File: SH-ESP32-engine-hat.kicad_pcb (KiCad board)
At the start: 4 copper layers, 34 x 52.8 mm, 106 parts, among them J301 Conn_02x04_Odd_Even, J302 Conn_02x04_Odd_Even, J401 I2C_top, J402 I2C_bottom, J403 GPIO subset, J501 Conn_02x04_Odd_Even, J502 Conn_02x04, Q501 S9015, Q502 S9015, Q503 S9015, Q504 S9015, U501 LMV324, U502 ADS1115IDGS

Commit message: Fix solder jumper silkscreen
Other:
- board text added: "0x48"
- board text added: "0x49"
- board text added: "0x4a"
- board text added: "0x4b"
- board text removed: "48"
- board text removed: "49"
- board text removed: "50"
- board text removed: "51"
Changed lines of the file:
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@@
     (effects (font (size 1 1) (thickness 0.16)) (justify mirror))
   )
-  (gr_text "I2C" (at 135.2 104.3) (layer "B.SilkS")
+  (gr_text "I2C" (at 135.4 104.3 270) (layer "B.SilkS")
     (effects (font (size 1 1) (thickness 0.2)) (justify mirror))
   )
@@
     (effects (font (size 0.8 0.8) (thickness 0.16)) (justify mirror))
   )
-  (gr_text "49" (at 131 97.8) (layer "B.SilkS")
+  (gr_text "0x49" (at 131 97.8) (layer "B.SilkS")
     (effects (font (size 0.8 0.8) (thickness 0.16)) (justify right mirror))
   )
-  (gr_text "51" (at 131 100.4) (layer "B.SilkS")
+  (gr_text "0x4b" (at 131 100.4) (layer "B.SilkS")
     (effects (font (size 0.8 0.8) (thickness 0.16)) (justify right mirror))
   )
-  (gr_text "48" (at 131.1 105.6) (layer "B.SilkS")
+  (gr_text "0x48" (at 131.1 105.6) (layer "B.SilkS")
     (effects (font (size 0.8 0.8) (thickness 0.16)) (justify right mirror))
   )
@@
     (effects (font (size 1 1) (thickness 0.2)) (justify mirror))
   )
-  (gr_text "50" (at 131 103) (layer "B.SilkS")
+  (gr_text "0x4a" (at 131 103) (layer "B.SilkS")
     (effects (font (size 0.8 0.8) (thickness 0.16)) (justify right mirror))
   )

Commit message: foo
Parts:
- moved J301 1.00 mm to (131.0, 81.3)
- moved J502 1.00 mm to (131.0, 94.0)
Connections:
- J401 pad 3: /Analog input/SCL -> /Analog input/ADDR
- J402 pad 3: /Analog input/SCL -> /Analog input/ADDR
- JP502 pad 2: /Analog input/SCL -> /Analog input/ADDR
- U502 pad 10: /Analog input/SCL -> /Analog input/ADDR
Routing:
- net /Analog input/ADDR: track 23.6 -> 52.2 mm, vias 1 -> 3
- net /Analog input/SCL: track 28.4 -> 0.00 mm, vias 2 -> 0
- net /Digital input/In4: track 6.06 -> 5.06 mm
- net /Digital input/In2: track 6.51 -> 5.51 mm
- net /Digital input/In1: track 6.88 -> 5.88 mm
- net /Analog input/InD: track 19.0 -> 18.0 mm
- net /Analog input/InC: track 18.4 -> 17.4 mm
- net /Analog input/InB: track 19.6 -> 18.6 mm
- net /Digital input/In3: track 6.06 -> 5.06 mm
- net /Analog input/InA: track 21.3 -> 20.7 mm
- net GND: vias 86 -> 72

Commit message: Add PCB graphics as symbols
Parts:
- removed the G*** at (154.3, 95.3)
- removed REF**: OSHW-Logo2_9.8x8mm_SilkScreen, Symbol:OSHW-Logo2_9.8x8mm_SilkScreen
- removed REF**: CE-Logo_11.2x8mm_SilkScreen, Symbol:CE-Logo_11.2x8mm_SilkScreen
- removed REF**: WEEE-Logo_5.6x8mm_SilkScreen, Symbol:WEEE-Logo_5.6x8mm_SilkScreen
- added G501: CC-BY, SH-ESP32-tank-hat:cc-by_5mm, B.Cu at (129.4, 64.3)
- added G502: CE-logo, Symbol:CE-Logo_11.2x8mm_SilkScreen, B.Cu at (139.4, 74.0)
- added G503: WEEE-logo, Symbol:WEEE-Logo_5.6x8mm_SilkScreen, B.Cu at (139.7, 83.8)
- added G504: OSHW-logo, Symbol:OSHW-Logo2_9.8x8mm_SilkScreen, B.Cu at (139.2, 92.1)
- added G505: HL-Logo, SH-ESP32-tank-hat:Hat_Labs_20mm, B.Cu at (154.3, 95.3)
- JP202: renamed from JP502; footprint Jumper:SolderJumper-2_P1.3mm_Bridged_Pad1.0x1.5mm -> Jumper:SolderJumper-2_P1.3mm_Bridged2Bar_RoundedPad1.0x1.5mm
- renumbered C501 to C201, C502 to C202, C503 to C203, C504 to C204, C505 to C205, C506 to C206, C507 to C207, C508 to C208, C509 to C209, C510 to C210, C511 to C211, C512 to C212, C513 to C213, C514 to C214, C515 to C215, C516 to C216, C517 to C217, C518 to C218, C519 to C219, C201 to C501, C202 to C502, C203 to C503, C204 to C504, C205 to C505, C206 to C506, C207 to C507, D501 to D201, D502 to D202, D503 to D203, D504 to D204, FB501 to FB201, FB502 to FB202, FB503 to FB203, FB504 to FB204, J501 to J201, J502 to J202, JP501 to JP201, JP503 to JP203, JP504 to JP204, Q501 to Q201, Q502 to Q202, Q503 to Q203, Q504 to Q204, R501 to R201, R502 to R202, R503 to R203, R504 to R204, R505 to R205, R506 to R206, R507 to R207, R508 to R208, R509 to R209, R510 to R210, R511 to R211, R512 to R212, R513 to R213, R514 to R214, R515 to R215, R516 to R216, R517 to R217, R518 to R218, U501 to U201, U502 to U202
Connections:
- J401 pad 3: /Analog input/ADDR -> /Analog input/SCL
- J402 pad 3: /Analog input/ADDR -> /Analog input/SCL
- JP202 pad 2: /Analog input/ADDR -> /Analog input/SCL
- U202 pad 10: /Analog input/ADDR -> /Analog input/SCL
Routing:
- net /Analog input/SCL: track 0.00 -> 28.4 mm, vias 0 -> 2
- net /Analog input/ADDR: track 52.2 -> 23.8 mm, vias 3 -> 1
- net GND: vias 72 -> 71
- net (no net): vias 1 -> 0

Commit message: Add panel tab annotations
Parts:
- removed G***: LOGO, SH-ESP32-tank-hat:cc-by_5mm
- added REF**: Tab, kikit:Tab, F.Cu at (125.8, 102.2)
- added REF**: Tab, kikit:Tab, F.Cu at (143.4, 56.8)
- added REF**: Tab, kikit:Tab, F.Cu at (160.2, 72.4)
- added REF**: Tab, kikit:Tab, F.Cu at (143.4, 110.0)

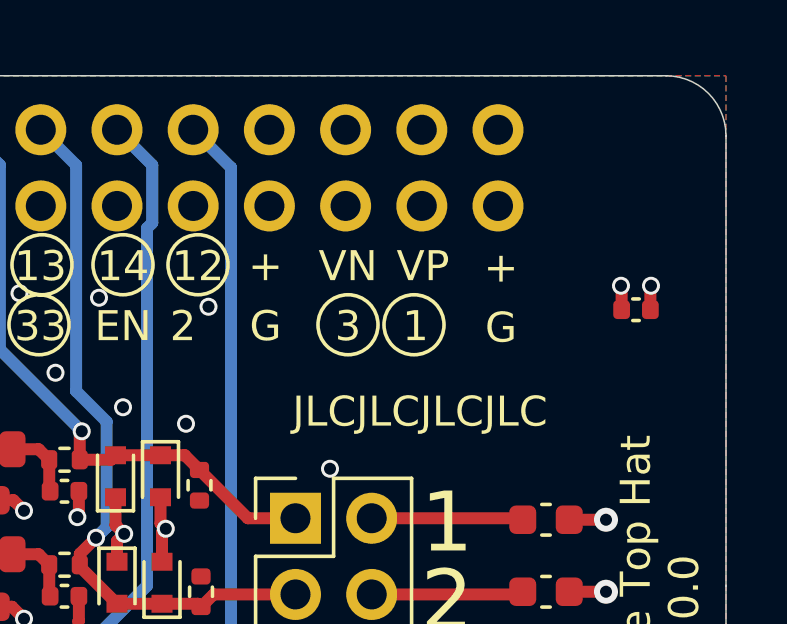
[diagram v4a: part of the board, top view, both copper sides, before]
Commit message: Refill zones, remove JLC order number template
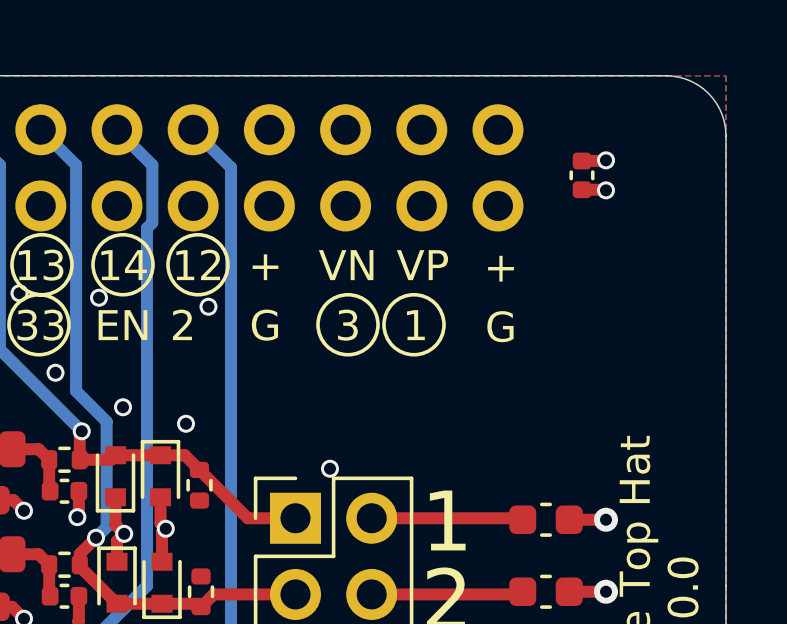
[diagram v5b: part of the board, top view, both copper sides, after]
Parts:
- moved C506 4.83 mm to (155.2, 60.3), turned to 90 degrees
- moved REF** 4.70 mm to (160.2, 67.7)
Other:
- board text removed: "JLCJLCJLCJLC"
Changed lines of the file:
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@@
   )
   (footprint "Capacitor_SMD:C_0402_1005Metric" (layer "F.Cu")
-    (at 157 64.8 180)
+    (at 155.2 60.32 90)
     (descr "Capacitor SMD 0402 (1005 Metric), square (rectangular) end terminal, IPC_7351 nominal, (Body size source: IPC-SM-782 page 76, https://www.pcb-3d.com/wordpress/wp-content/uploads/ipc-sm-782a_amendment_1_and_2.pdf), generated with kicad-footprint-generator")
     (tags "capacitor")
@@
     (property "Sheetname" "PCB")
     (attr smd)
-    (fp_text reference "C506" (at 0 -1.16) (layer "F.SilkS") hide
+    (fp_text reference "C506" (at 0 -1.16 90) (layer "F.SilkS") hide
       (effects (font (size 1 1) (thickness 0.15)))
     )
-    (fp_text value "100nF" (at 0 1.16) (layer "F.Fab") hide
+    (fp_text value "100nF" (at 0 1.16 90) (layer "F.Fab") hide
       (effects (font (size 1 1) (thickness 0.15)))
     )
-    (fp_text user "${REFERENCE}" (at 0 0) (layer "F.Fab") hide
+    (fp_text user "${REFERENCE}" (at 0 0 90) (layer "F.Fab") hide
       (effects (font (size 0.25 0.25) (thickness 0.04)))
     )
@@
     (fp_line (start -0.5 -0.25) (end 0.5 -0.25) (layer "F.Fab") (width 0.1))
     (fp_line (start 0.5 -0.25) (end 0.5 0.25) (layer "F.Fab") (width 0.1))
-    (pad "1" smd roundrect locked (at -0.48 0 180) (size 0.56 0.62) (layers "F.Cu" "F.Paste" "F.Mask") (roundrect_rratio 0.25)
+    (pad "1" smd roundrect locked (at -0.48 0 90) (size 0.56 0.62) (layers "F.Cu" "F.Paste" "F.Mask") (roundrect_rratio 0.25)
       (net 1 "GND") (pintype "passive"))
-    (pad "2" smd roundrect locked (at 0.48 0 180) (size 0.56 0.62) (layers "F.Cu" "F.Paste" "F.Mask") (roundrect_rratio 0.25)
+    (pad "2" smd roundrect locked (at 0.48 0 90) (size 0.56 0.62) (layers "F.Cu" "F.Paste" "F.Mask") (roundrect_rratio 0.25)
       (net 2 "+3V3") (pintype "passive"))
     (model "${KICAD6_3DMODEL_DIR}/Capacitor_SMD.3dshapes/C_0402_1005Metric.wrl"
@@
   )
   (footprint "kikit:Tab" (layer "F.Cu")
-    (at 160.25 72.4 180)
+    (at 160.25 67.7 180)
     (descr "A symbol representing annotation for tab placement")
     (attr board_only exclude_from_pos_files exclude_from_bom)
@@
     (effects (font (size 1.5 1.5) (thickness 0.3)) (justify left))
   )
-  (gr_text "JLCJLCJLCJLC" (at 149.8 68.2) (layer "F.SilkS")
-    (effects (font (size 1 1) (thickness 0.16)))
-  )
   (gr_text "2" (at 132.7 76.3) (layer "F.SilkS")
     (effects (font (size 2 2) (thickness 0.3)))
@@
   (segment (start 138.46 82.26) (end 138.5 82.3) (width 0.4) (layer "F.Cu") (net 1))
   (segment (start 139.95 88.92) (end 139.38 88.92) (width 0.4) (layer "F.Cu") (net 1))
-  (segment (start 157.48 64.02) (end 157.5 64) (width 0.4) (layer "F.Cu") (net 1))
+  (segment (start 155.98 60.8) (end 156 60.82) (width 0.4) (layer "F.Cu") (net 1))
   (segment (start 138.46 81.4) (end 138.46 82.26) (width 0.4) (layer "F.Cu") (net 1))
   (segment (start 153.95 104.775) (end 153.95 106.35) (width 0.4) (layer "F.Cu") (net 1))
@@
   (segment (start 147.98 99.88) (end 148 99.9) (width 0.4) (layer "F.Cu") (net 1))
   (segment (start 140.95 84.32) (end 141.62 84.32) (width 0.4) (layer "F.Cu") (net 1))
-  (segment (start 157.48 64.8) (end 157.48 64.02) (width 0.4) (layer "F.Cu") (net 1))
+  (segment (start 155.2 60.8) (end 155.98 60.8) (width 0.4) (layer "F.Cu") (net 1))
   (segment (start 146.05 101.35) (end 146 101.4) (width 0.4) (layer "F.Cu") (net 1))
   (segment (start 141.62 84.32) (end 141.7 84.4) (width 0.4) (layer "F.Cu") (net 1))
@@
   (via (at 132.9 70.8) (size 0.6) (drill 0.4) (layers "F.Cu" "B.Cu") (net 1))
   (via (at 136.7 82.3) (size 0.6) (drill 0.4) (layers "F.Cu" "B.Cu") (net 1))
-  (via (at 157.5 64) (size 0.6) (drill 0.4) (layers "F.Cu" "B.Cu") (net 1))
+  (via (at 156 60.82) (size 0.6) (drill 0.4) (layers "F.Cu" "B.Cu") (net 1))
   (via (at 127.5 108.2) (size 0.6) (drill 0.4) (layers "F.Cu" "B.Cu") (net 1))
   (via (at 143.65 93.85) (size 0.6) (drill 0.4) (layers "F.Cu" "B.Cu") (net 1))
@@
   (segment (start 127.519996 107.22) (end 127.5 107.200004) (width 0.4) (layer "F.Cu") (net 2))
   (segment (start 152 82.78) (end 151.22 82.78) (width 0.4) (layer "F.Cu") (net 2))
-  (segment (start 156.52 64.02) (end 156.5 64) (width 0.4) (layer "F.Cu") (net 2))
+  (segment (start 155.98 59.84) (end 156 59.82) (width 0.4) (layer "F.Cu") (net 2))
   (segment (start 132.5 69.78) (end 131.72 69.78) (width 0.4) (layer "F.Cu") (net 2))
   (segment (start 139.65 71.05) (end 139.65 71.980028) (width 0.4) (layer "F.Cu") (net 2))
@@
   (segment (start 157 94.32) (end 158.234012 94.32) (width 0.4) (layer "F.Cu") (net 2))
   (segment (start 139.7 73.2) (end 139.7 72.509492) (width 0.4) (layer "F.Cu") (net 2))
-  (segment (start 156.52 64.8) (end 156.52 64.02) (width 0.4) (layer "F.Cu") (net 2))
+  (segment (start 155.2 59.84) (end 155.98 59.84) (width 0.4) (layer "F.Cu") (net 2))
   (segment (start 157.1 90.22) (end 158.534012 90.22) (width 0.4) (layer "F.Cu") (net 2))
   (segment (start 139.7 72.509492) (end 139.939732 72.26976) (width 0.4) (layer "F.Cu") (net 2))
@@
   (via (at 131.7 69.8) (size 0.6) (drill 0.4) (layers "F.Cu" "B.Cu") (net 2))
   (via (at 155.3 107.3) (size 0.6) (drill 0.4) (layers "F.Cu" "B.Cu") (net 2))
-  (via (at 156.5 64) (size 0.6) (drill 0.4) (layers "F.Cu" "B.Cu") (net 2))
+  (via (at 156 59.82) (size 0.6) (drill 0.4) (layers "F.Cu" "B.Cu") (net 2))
   (via (at 143.4 100.6) (size 0.6) (drill 0.4) (layers "F.Cu" "B.Cu") (net 2))
   (via (at 130.3 97.7) (size 0.6) (drill 0.4) (layers "F.Cu" "B.Cu") (net 2))

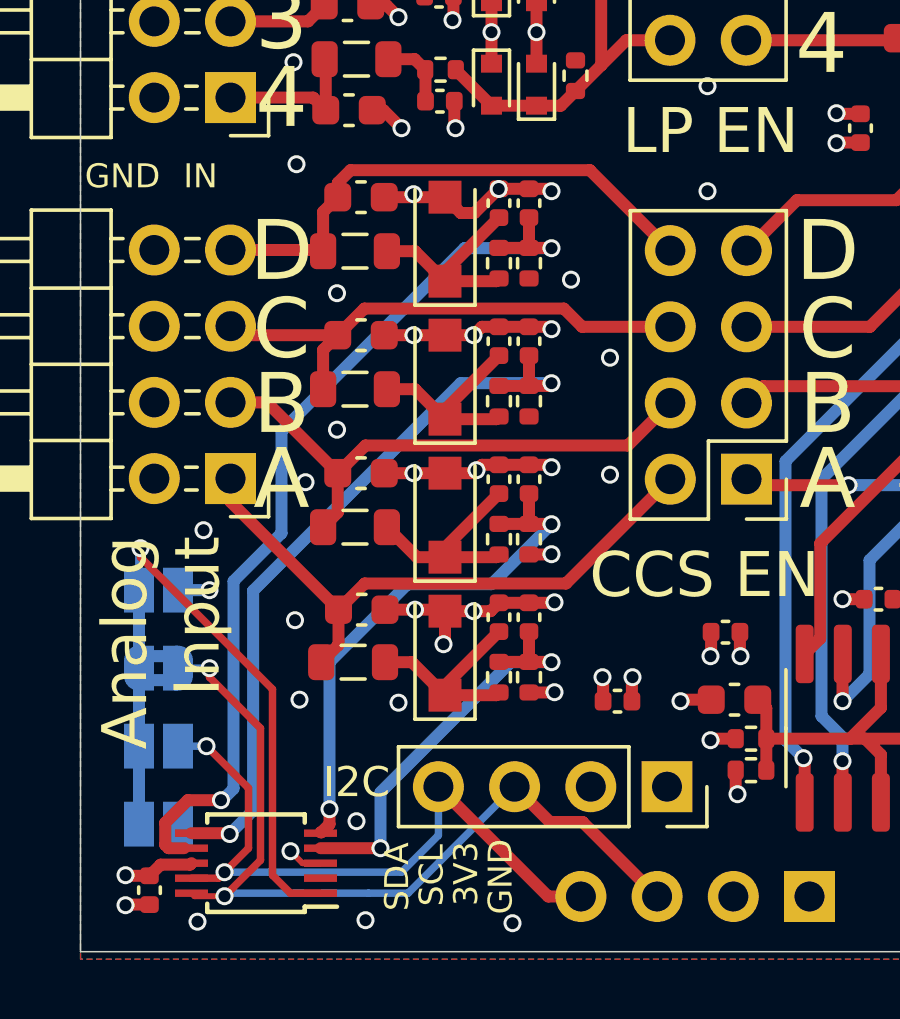
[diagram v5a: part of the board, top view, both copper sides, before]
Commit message: Replace C211-214 with 50V 0603 footprint parts
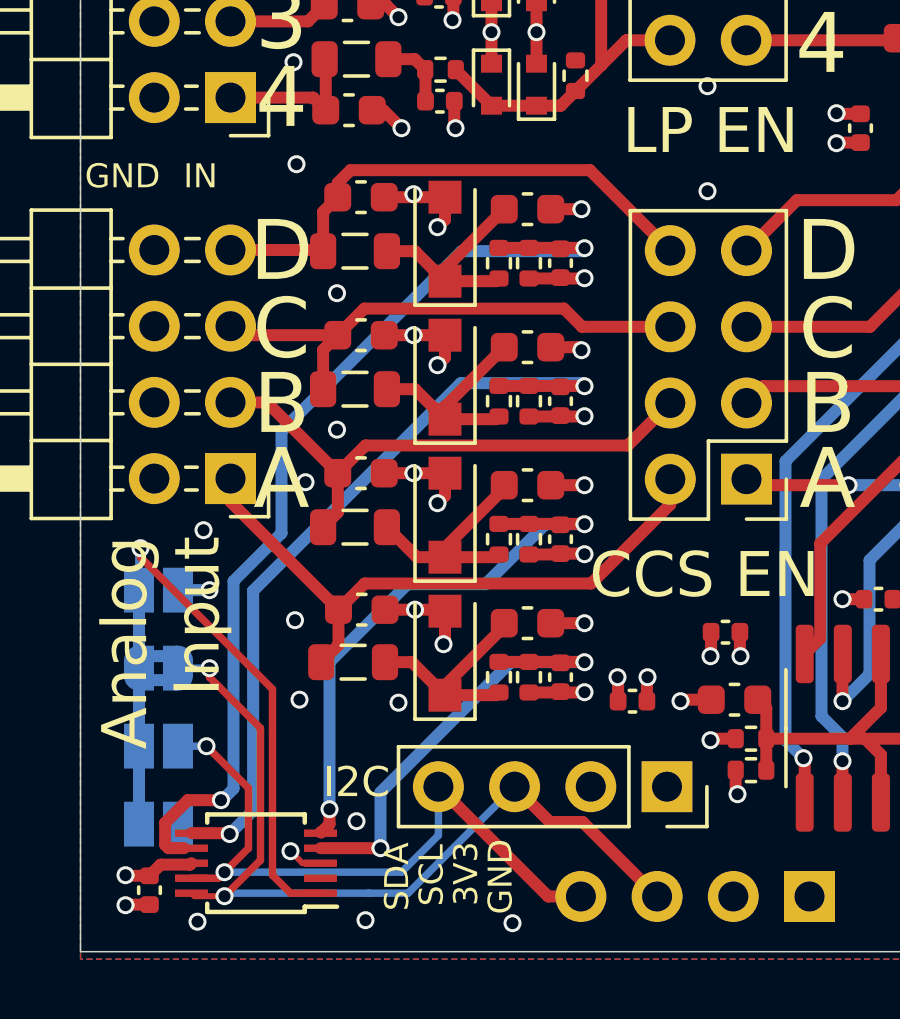
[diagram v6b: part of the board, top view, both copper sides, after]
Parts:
- C207, C208, C209, C210: value 1uF -> 1uF/50V
- C211, C212, C213, C214: value 1uF -> 1uF/50V; footprint Capacitor_SMD:C_0402_1005Metric -> Capacitor_SMD:C_0603_1608Metric
- moved C215 2.26 mm to (142.0, 100.6), turned to -90 degrees
- moved C216 2.26 mm to (142.0, 96.0), turned to -90 degrees
- moved C217 2.26 mm to (142.0, 91.4), turned to -90 degrees
- moved C218 2.26 mm to (142.0, 86.8), turned to -90 degrees
- moved C211 0.97 mm to (140.9, 98.8), turned to 0 degrees
- moved C212 0.97 mm to (140.9, 94.2), turned to 0 degrees
- moved C214 0.97 mm to (140.9, 85.0), turned to 0 degrees
- moved C213 0.97 mm to (140.9, 89.6), turned to 0 degrees
- moved C502 0.50 mm to (144.4, 101.4)
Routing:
- net GND: track 55.3 -> 53.5 mm, vias 71 -> 69
- net /Analog input/ADC_C: track 25.3 -> 26.5 mm
- net /Analog input/ADC_B: track 17.9 -> 19.1 mm
- net /Analog input/ADC_A: track 14.1 -> 15.3 mm
- net /Analog input/ADC_D: track 31.0 -> 32.2 mm

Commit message: Update sheet data; refill
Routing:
- net GND: vias 69 -> 70
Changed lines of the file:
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@@
   (title_block
     (title "Engine Top Hat for SH-ESP32")
-    (date "2021-12-31")
+    (date "2022-02-03")
     (rev "1.0.0")
     (company "Hat Labs Ltd")
@@
     (effects (font (size 2 2) (thickness 0.3)))
   )
-  (gr_text "CCS EN" (at 146.8 97.2) (layer "F.SilkS")
+  (gr_text "CCS EN" (at 147 97.2) (layer "F.SilkS")
     (effects (font (size 1.5 1.5) (thickness 0.3)))
   )
@@
   (segment (start 155.2 60.8) (end 155.98 60.8) (width 0.4) (layer "F.Cu") (net 1))
   (segment (start 146.05 101.35) (end 146 101.4) (width 0.4) (layer "F.Cu") (net 1))
-  (segment (start 138.43 75.17) (end 138.4 75.2) (width 0.4) (layer "F.Cu") (net 1))
   (segment (start 142.79 87.31) (end 142.8 87.3) (width 0.4) (layer "F.Cu") (net 1))
   (segment (start 154.775 71.8) (end 156 71.8) (width 0.4) (layer "F.Cu") (net 1))
@@
   (segment (start 141.15 71.92299) (end 141.32701 72.1) (width 0.4) (layer "F.Cu") (net 1))
   (segment (start 147.025 101.35) (end 146.05 101.35) (width 0.4) (layer "F.Cu") (net 1))
+  (segment (start 138.4 75.2) (end 138.43 75.17) (width 0.4) (layer "F.Cu") (net 1))
   (segment (start 138.43 78.67) (end 138.4 78.7) (width 0.4) (layer "F.Cu") (net 1))
   (segment (start 138.1 98.35) (end 138.15 98.4) (width 0.4) (layer "F.Cu") (net 1))
@@
   (via (at 146.9 84.4) (size 0.6) (drill 0.4) (layers "F.Cu" "B.Cu") (net 1))
   (via (at 136.6 101.45) (size 0.6) (drill 0.4) (layers "F.Cu" "B.Cu") (net 1))
+  (via (at 138.43 75.17) (size 0.6) (drill 0.4) (layers "F.Cu" "B.Cu") (net 1))
   (via (at 133.2 77.4) (size 0.6) (drill 0.4) (layers "F.Cu" "B.Cu") (net 1))
   (via (at 130.1 95.7) (size 0.6) (drill 0.4) (layers "F.Cu" "B.Cu") (net 1))
